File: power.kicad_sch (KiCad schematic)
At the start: 23 parts, among them IC3 CYPD3177-24LQXQ, IC4 DMP3013SFV-7, IC5 DMP3013SFV-7, IC6 DMP3013SFV-7, IC7 DMP3013SFV-7, IC8 LT8653SEV#PBF, J2 USB_C_Receptacle_PowerOnly_24P

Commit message: Added PD, need to work on a power mux and regulator
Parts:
- added IC9: TPS2121RUXT, TPS2121RUXT, symbol SamacSys_Parts:TPS2121RUXT
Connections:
- new net IN1: IC9.7 (IN1)
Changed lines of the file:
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@@
 	(label "ISNK_COARSE"
 		(at 99.06 76.2 0)
+		(fields_autoplaced yes)
 		(effects
 			(font
@@
 	(label "VBUS_MIN"
 		(at 99.06 66.04 0)
+		(fields_autoplaced yes)
 		(effects
 			(font
@@
 	(label "ISNK_FINE"
 		(at 99.06 78.74 0)
+		(fields_autoplaced yes)
 		(effects
 			(font
@@
 	(label "VBUS_MAX"
 		(at 99.06 68.58 0)
+		(fields_autoplaced yes)
 		(effects
 			(font
@@
 		(shape input)
 		(at 58.42 78.74 180)
+		(fields_autoplaced yes)
+		(effects
+			(font
+				(size 1.27 1.27)
+			)
+			(justify right)
+		)
+	)
+	(hierarchical_label "IN1"
+		(shape input)
+		(at 34.29 161.29 180)
 		(effects
 			(font
@@
 		(shape input)
 		(at 73.66 99.06 270)
+		(fields_autoplaced yes)
 		(effects
 			(font
@@
 					(unit 1)
 				)
+			)
+		)
+	)
+	(symbol
+		(lib_id "SamacSys_Parts:TPS2121RUXT")
+		(at 34.29 161.29 0)
+		(unit 1)
+		(exclude_from_sim no)
+		(in_bom yes)
+		(on_board yes)
+		(dnp no)
+		(fields_autoplaced yes)
+		(property "Reference" "IC9"
+			(at 48.26 191.77 0)
+			(effects
+				(font
+					(size 1.27 1.27)
+				)
+			)
+		)
+		(property "Value" "TPS2121RUXT"
+			(at 48.26 194.31 0)
+			(effects
+				(font
+					(size 1.27 1.27)
+				)
+			)
+		)
+		(property "Footprint" "TPS2121RUXT"
+			(at 58.42 248.59 0)
+			(effects
+				(font
+					(size 1.27 1.27)
+				)
+				(justify left top)
+				(hide yes)
+			)
+		)
+		(property "Datasheet" "https://www.arrow.com/en/products/tps2121ruxt/texas-instruments"
+			(at 58.42 348.59 0)
+			(effects
+				(font
+					(size 1.27 1.27)
+				)
+				(justify left top)
+				(hide yes)
+			)
+		)
+		(property "Description" "Power Switch ICs - Power Distribution 2.7-22V, 56mG , 4.5A, Priority Power MUX with Seamless Switchover 12-VQFN-HR -40 to 125"
+			(at 34.29 161.29 0)
+			(effects
+				(font
+					(size 1.27 1.27)
+				)
+				(hide yes)
+			)
+		)
+		(property "Height" "1"
+			(at 58.42 548.59 0)
+			(effects
+				(font
+					(size 1.27 1.27)
+				)
+				(justify left top)
+				(hide yes)
+			)
+		)
+		(property "Mouser Part Number" "595-TPS2121RUXT"
+			(at 58.42 648.59 0)
+			(effects
+				(font
+					(size 1.27 1.27)
+				)
+				(justify left top)
+				(hide yes)
+			)
+		)
+		(property "Mouser Price/Stock" "https://www.mouser.co.uk/ProductDetail/Texas-Instruments/TPS2121RUXT?qs=l7cgNqFNU1i6abJCbO5ulQ%3D%3D"
+			(at 58.42 748.59 0)
+			(effects
+				(font
+					(size 1.27 1.27)
+				)
+				(justify left top)
+				(hide yes)
+			)
+		)
+		(property "Manufacturer_Name" "Texas Instruments"
+			(at 58.42 848.59 0)
+			(effects
+				(font
+					(size 1.27 1.27)
+				)
+				(justify left top)
+				(hide yes)
+			)
+		)
+		(property "Manufacturer_Part_Number" "TPS2121RUXT"
+			(at 58.42 948.59 0)
+			(effects
+				(font
+					(size 1.27 1.27)
+				)
+				(justify left top)
+				(hide yes)
+			)
+		)
+		(pin "6"
+		)
+		(pin "9"
+		)
+		(pin "2"
+		)
+		(pin "5"
+		)
+		(pin "1"
+		)
+		(pin "11"
+		)
+		(pin "7"
+		)
+		(pin "4"
+		)
+		(pin "12"
+		)
+		(pin "10"
+		)
+		(pin "3"
+		)
+		(pin "8"
+		)
+		(instances
+			(project ""
+				(path "/9ba02813-5189-4482-9c9e-35a29bc7aded/91878a69-aab9-40cd-8e36-3035ed8b91de"
+					(reference "IC9")
+					(unit 1)
+				)

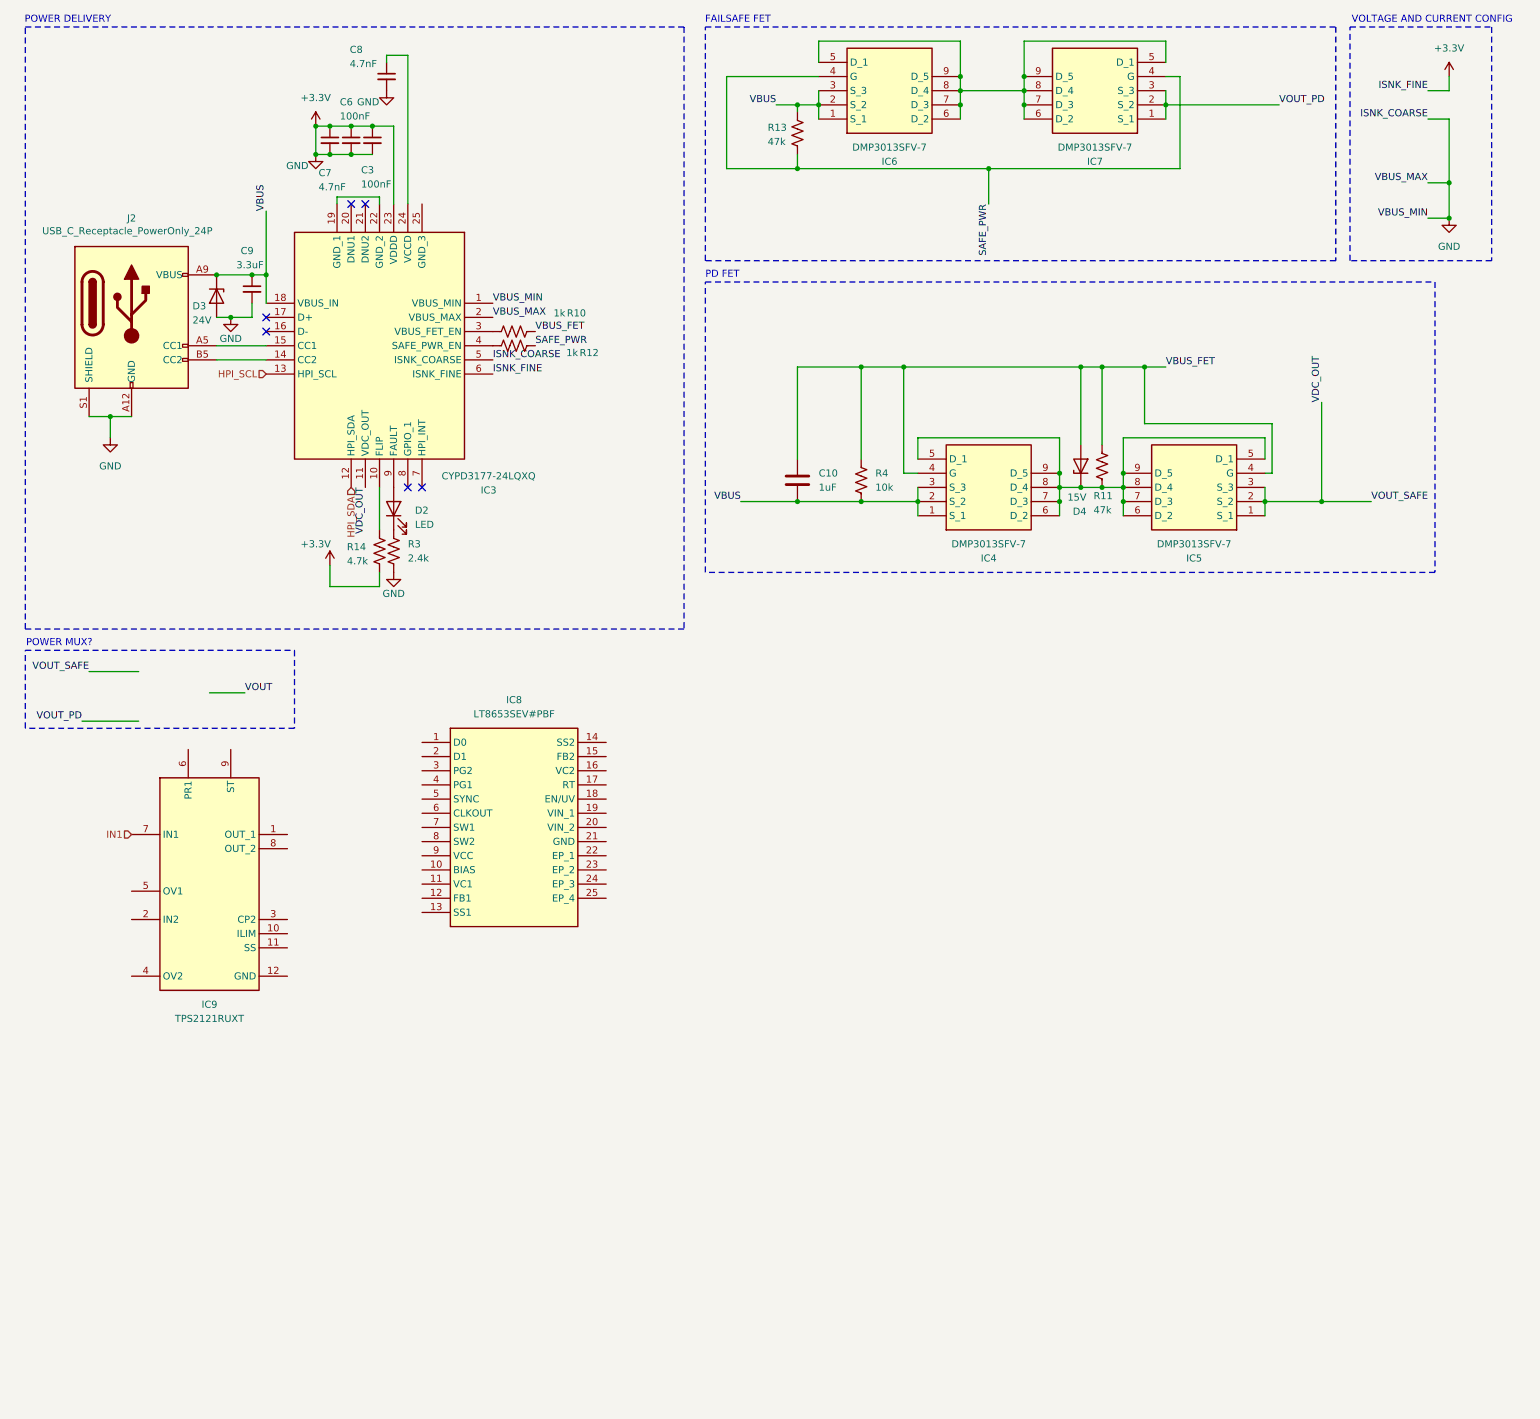
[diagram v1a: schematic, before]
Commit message: added power mux
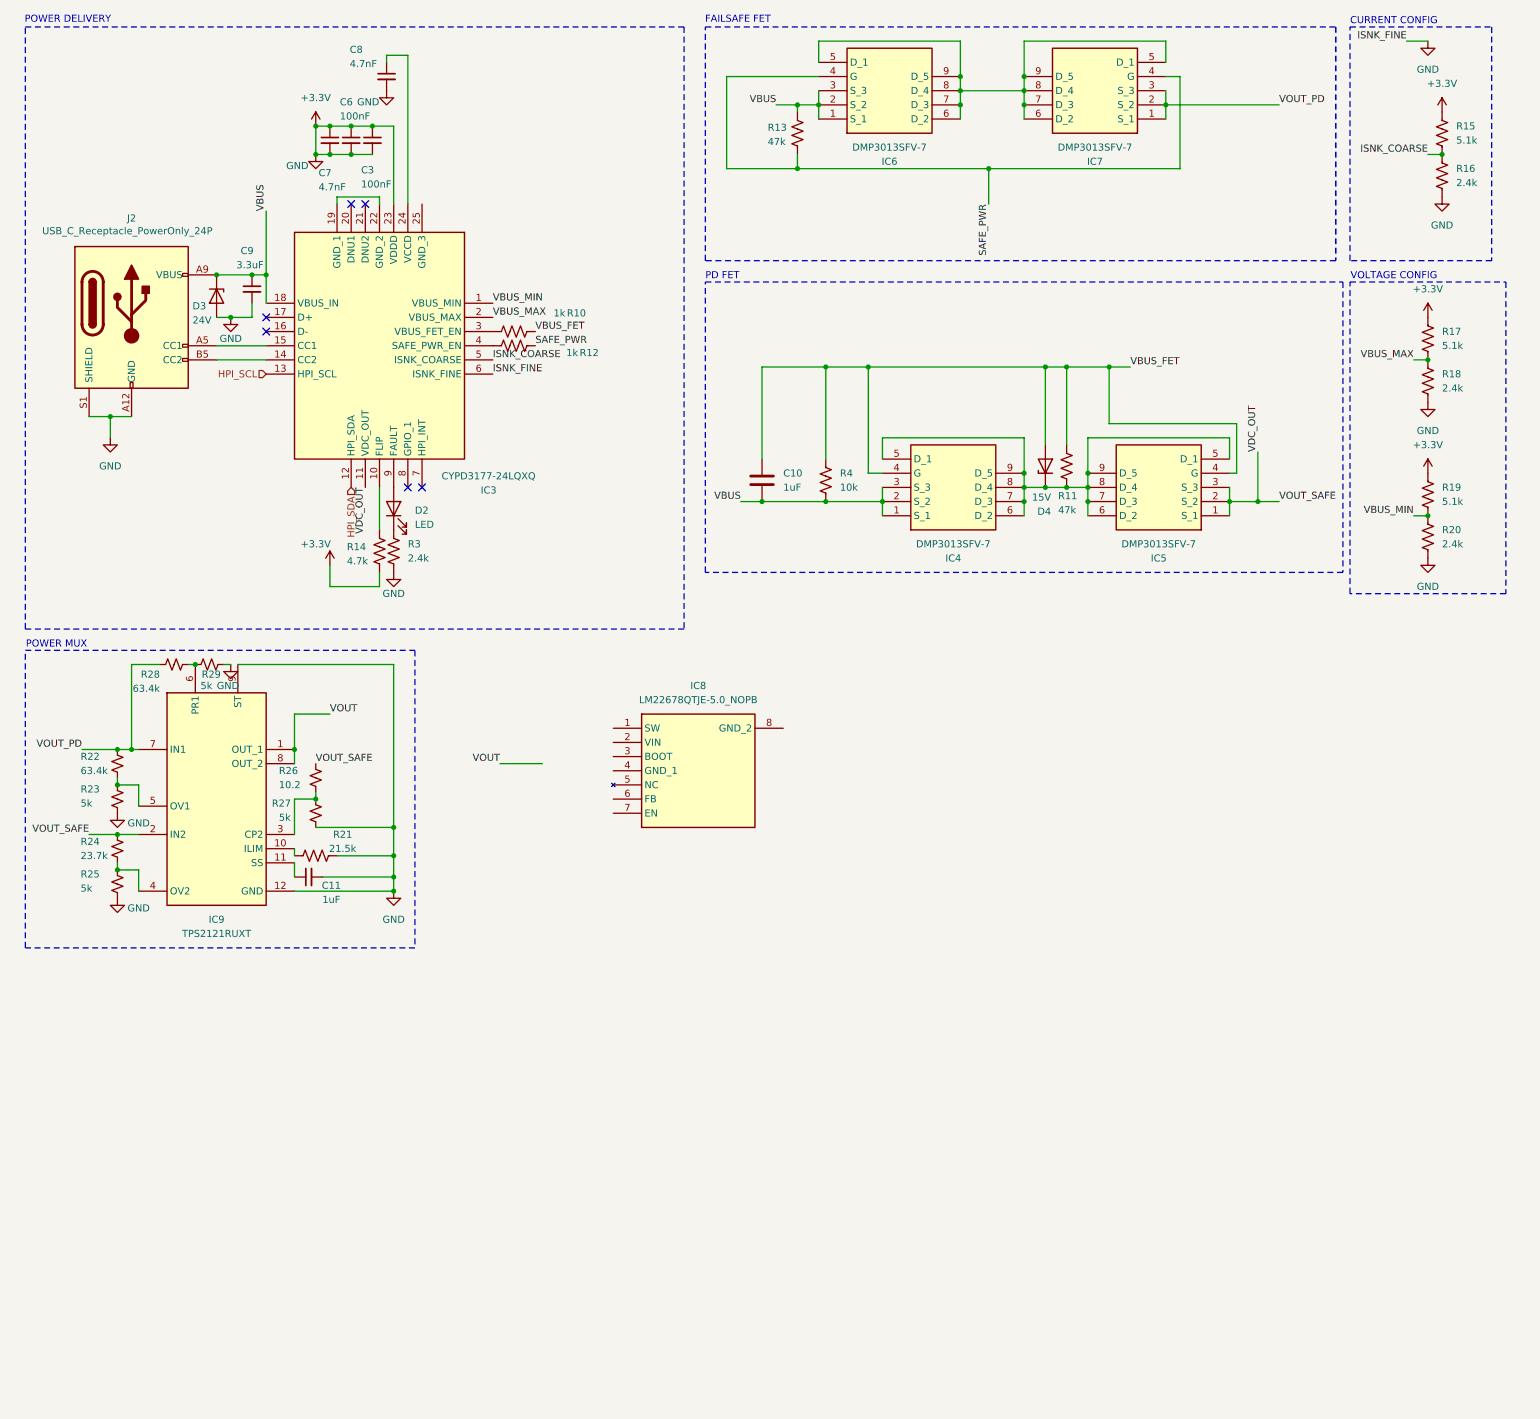
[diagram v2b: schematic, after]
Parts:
- removed IC8: LT8653SEV#PBF, LT8653SEVPBF, symbol SamacSys_Parts:LT8653SEV#PBF
- added C11: 1uF, symbol Device:C_Small
- added IC8: LM22678QTJE-5.0_NOPB, LM22678QTJE50NOPB, symbol SamacSys_Parts:LM22678QTJE-5.0_NOPB
- added R15, R17, R19: 5.1k, symbol Device:R_US
- added R16, R18, R20: 2.4k, symbol Device:R_US
- added R21: 21.5k, symbol Device:R_US
- added R22, R28: 63.4k, symbol Device:R_Small_US
- added R23, R25, R27, R29: 5k, symbol Device:R_Small_US
- added R24: 23.7k, symbol Device:R_Small_US
- added R26: 10.2, symbol Device:R_Small_US
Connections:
- net IN1 is gone; now on net VOUT_PD: IC9.7 (IN1)
- net +3.3V: now also IC9.12 (GND), IC9.9 (ST), C11.2, R15.1, R16.2, R17.1, R18.2, R19.1, R20.2, R21.2, R23.2, R25.2, R27.2, R29.2; no longer IC3.1 (VBUS_MIN), IC3.2 (VBUS_MAX), IC3.5 (ISNK_COARSE)
- net VDC_OUT: now also IC9.2 (IN2), R24.1, R26.1
- net VOUT: now also IC9.1 (OUT_1), IC9.8 (OUT_2)
- net VOUT_PD: now also R22.1, R28.1
- net at IC9.10 (ILIM): now also R21.1
- net at IC9.11 (SS): now also C11.1
- net at IC9.3 (CP2): now also R26.2, R27.1
- net at IC9.4 (OV2): now also R24.2, R25.1
- net at IC9.5 (OV1): now also R22.2, R23.1
- net at IC9.6 (PR1): now also R28.2, R29.1
- new net ISNK_COARSE: IC3.5 (ISNK_COARSE), R15.2, R16.1
- new net VBUS_MAX: IC3.2 (VBUS_MAX), R17.2, R18.1
- new net VBUS_MIN: IC3.1 (VBUS_MIN), R19.2, R20.1
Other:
- note added: "CURRENT CONFIG"
- note added: "POWER MUX"
- note added: "VOLTAGE CONFIG"
- note removed: "POWER MUX?"
- note removed: "VOLTAGE AND CURRENT CONFIG"
- moved on the sheet: C10, D4, IC4, IC5, IC9, R11, R4

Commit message: POWER IS DONE!!! need someone to check it
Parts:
- removed IC8: LM22678QTJE-5.0_NOPB, LM22678QTJE50NOPB, symbol SamacSys_Parts:LM22678QTJE-5.0_NOPB
- removed IC9: TPS2121RUXT, TPS2121RUXT, symbol SamacSys_Parts:TPS2121RUXT
- removed R15, R17, R19: 5.1k, symbol Device:R_US
- removed R16, R18, R20: 2.4k, symbol Device:R_US
- removed R21: 21.5k, symbol Device:R_US
- removed R22, R28: 63.4k, symbol Device:R_Small_US
- removed R23, R25, R27, R29: 5k, symbol Device:R_Small_US
- removed R24: 23.7k, symbol Device:R_Small_US
- removed R26: 10.2, symbol Device:R_Small_US
- added C12: 10uF 25V, symbol Device:C_Small
- added C13, C14: 22uF 25V, symbol Device:C_Small
- added C15: 2.2uF 10V, symbol Device:C_Small
- added C16, C17: 0.22uF 25V, symbol Device:C_Small
- added C18: 0.47uF 6.3V, symbol Device:C_Small
- added D5, D6: PMEG045V100EPE-QZ, PMEG045V100EPEQZ, symbol SamacSys_Parts:PMEG045V100EPE-QZ
- added IC10: LMS1585AISX-3.3_NO, KTT0003B, symbol SamacSys_Parts:LMS1585AISX-3.3_NO
- added IC8: MAX77857CEWB+T, BGA35C40P7X5_283X203X69, symbol SamacSys_Parts:MAX77857CEWB+T
- added IC9: TPS73616DBVR, SOT95P280X145-5N, symbol SamacSys_Parts:TPS73616DBVR
- added J3: Conn_01x02_Pin, symbol Connector:Conn_01x02_Pin
- added L1: 1.5uH, symbol Device:L
- C11: value 1uF -> 10uF 25V
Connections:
- net ISNK_COARSE is gone; now on net +3.3V: IC3.5 (ISNK_COARSE)
- net VBUS_MAX is gone; now on net +3.3V: IC3.2 (VBUS_MAX)
- net VBUS_MIN is gone; now on net +3.3V: IC3.1 (VBUS_MIN)
- net +3.3V: now also C12.2, C13.2, C14.2, C15.2, C18.2, IC10.1 (ADJ/GND), IC10.4 (VOUT), IC8.C3 (PGND_1), IC8.C4 (PGND_2), IC8.C5 (PGND_3), IC8.C6 (PGND_4), IC8.C7 (PGND_5), IC8.D2 (PGND_6), IC8.D3 (PGND_7), IC8.E2 (AGND), IC9.2 (GND), J3.2 (Pin_2)
- net VDC_OUT: now also D6.1 (A_1), D6.2 (A_2)
- net VOUT: now also C11.1, C12.1, D5.3 (K), D6.3 (K), IC8.A4 (IN_1), IC8.A5 (IN_2), IC8.A6 (IN_3), IC8.B4 (IN_4), IC9.1 (IN), IC9.3 (EN), J3.1 (Pin_1)
- net VOUT_PD: now also D5.1 (A_1), D5.2 (A_2)
- new net: C15.1, IC8.C1 (VL)
- new net +5V: C13.1, C14.1, IC10.3 (INPUT), IC8.D4 (OUT_1), IC8.E1 (FB), IC8.E4 (OUT_2), IC8.E5 (OUT_3), IC8.E6 (OUT_4)
- new net BST1: C16.2, IC8.A3 (BST1)
- new net BST2: C17.2, IC8.E3 (BST2)
- new net EN: IC8.B2 (EN_1), IC8.B3 (EN_2)
- new net LX1: C16.1, IC8.A7 (LX1_1), IC8.B5 (LX1_2), IC8.B6 (LX1_3), IC8.B7 (LX1_4), L1.1
- new net LX2: C17.1, IC8.D5 (LX2_1), IC8.D6 (LX2_2), IC8.D7 (LX2_3), IC8.E7 (LX2_4), L1.2
- new net VOUT_1.8: C18.1, IC8.A2 (VIO), IC9.5 (OUT)
- no-connect marks 6 -> 10
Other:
- note added: "3.3V UP TO 5A"
- note added: "CONFIG"
- note added: "STABILZE USB INPUT TO 5V"
- note added: "VOUT MERGE AND BATTERY SUPPORT"
- note added: "VOUT TO 1.8"
- note removed: "CURRENT CONFIG"
- note removed: "POWER MUX"
- note removed: "VOLTAGE CONFIG"

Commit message: Used steppenprobe as base for our UART and JTAG.
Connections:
- net VOUT_1.8 renamed +1V8
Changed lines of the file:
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@@
 	(label "BST2"
 		(at 110.49 205.74 0)
+		(fields_autoplaced yes)
 		(effects
 			(font
@@
 		)
 	)
-	(label "VOUT_1.8"
-		(at 25.4 177.8 180)
-		(fields_autoplaced yes)
-		(effects
-			(font
-				(size 1.27 1.27)
-			)
-			(justify right bottom)
-		)
-	)
 	(label "ISNK_COARSE"
 		(at 99.06 76.2 0)
@@
 	(label "BST1"
 		(at 66.04 180.34 180)
+		(fields_autoplaced yes)
 		(effects
 			(font
@@
 		)
 	)
-	(label "VOUT_1.8"
-		(at 128.27 138.43 0)
-		(fields_autoplaced yes)
-		(effects
-			(font
-				(size 1.27 1.27)
-			)
-			(justify left bottom)
-		)
-	)
 	(label "VOUT"
 		(at 45.72 186.69 180)
@@
 	)
 	(symbol
+		(lib_id "power:+1V8")
+		(at 128.27 138.43 0)
+		(unit 1)
+		(exclude_from_sim no)
+		(in_bom yes)
+		(on_board yes)
+		(dnp no)
+		(fields_autoplaced yes)
+		(property "Reference" "#PWR013"
+			(at 128.27 142.24 0)
+			(effects
+				(font
+					(size 1.27 1.27)
+				)
+				(hide yes)
+			)
+		)
+		(property "Value" "+1V8"
+			(at 128.27 133.35 0)
+			(effects
+				(font
+					(size 1.27 1.27)
+				)
+			)
+		)
+		(property "Footprint" ""
+			(at 128.27 138.43 0)
+			(effects
+				(font
+					(size 1.27 1.27)
+				)
+				(hide yes)
+			)
+		)
+		(property "Datasheet" ""
+			(at 128.27 138.43 0)
+			(effects
+				(font
+					(size 1.27 1.27)
+				)
+				(hide yes)
+			)
+		)
+		(property "Description" "Power symbol creates a global label with name \"+1V8\""
+			(at 128.27 138.43 0)
+			(effects
+				(font
+					(size 1.27 1.27)
+				)
+				(hide yes)
+			)
+		)
+		(pin "1"
+		)
+		(instances
+			(project ""
+				(path "/9ba02813-5189-4482-9c9e-35a29bc7aded/91878a69-aab9-40cd-8e36-3035ed8b91de"
+					(reference "#PWR013")
+					(unit 1)
+				)
+			)
+		)
+	)
+	(symbol
 		(lib_id "SamacSys_Parts:CYPD3177-24LQXQ")
 		(at 99.06 66.04 0)
@@
 					(unit 1)
 				)
+			)
+		)
+	)
+	(symbol
+		(lib_id "power:+1V8")
+		(at 25.4 177.8 0)
+		(unit 1)
+		(exclude_from_sim no)
+		(in_bom yes)
+		(on_board yes)
+		(dnp no)
+		(fields_autoplaced yes)
+		(property "Reference" "#PWR014"
+			(at 25.4 181.61 0)
+			(effects
+				(font
+					(size 1.27 1.27)
+				)
+				(hide yes)
+			)
+		)
+		(property "Value" "+1V8"
+			(at 25.4 172.72 0)
+			(effects
+				(font
+					(size 1.27 1.27)
+				)
+			)
+		)
+		(property "Footprint" ""
+			(at 25.4 177.8 0)
+			(effects
+				(font
+					(size 1.27 1.27)
+				)
+				(hide yes)
+			)
+		)
+		(property "Datasheet" ""
+			(at 25.4 177.8 0)
+			(effects
+				(font
+					(size 1.27 1.27)
+				)
+				(hide yes)
+			)
+		)
+		(property "Description" "Power symbol creates a global label with name \"+1V8\""
+			(at 25.4 177.8 0)
+			(effects
+				(font
+					(size 1.27 1.27)
+				)
+				(hide yes)
+			)
+		)
+		(pin "1"
+		)
+		(instances
+			(project "debug_board"
+				(path "/9ba02813-5189-4482-9c9e-35a29bc7aded/91878a69-aab9-40cd-8e36-3035ed8b91de"
+					(reference "#PWR014")
+					(unit 1)
+				)
